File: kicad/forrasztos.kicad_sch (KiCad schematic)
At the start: 58 parts, among them J1 Conn_01x04_Pin, J2 24V+-, J3 Conn_01x06_Pin, J4 Conn_01x20_Pin, Q1 PMOS, Q2 NPN, SW1 RotaryEncoder_Switch, U1 STM32F103C8Tx, U2 24LC00, U3 MCP601R, U4 ATA00A18S-L, U5 AP1117-33, U6 MCP601R, U7 MCP601R, Y1 8 MHz

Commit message: schematic mostly done
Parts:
- removed D3: LED, symbol Device:LED
- removed R14, R15: 10k, symbol Device:R
- removed R16: 470k, symbol Device:R
- removed R17, R19: 1k, symbol Device:R
- removed R18: 4k7, symbol Device:R
- removed R6: 10, symbol Device:R
- removed U3, U6, U7: MCP601R, Package_TO_SOT_SMD:SOT-23-5, symbol Amplifier_Operational:MCP601R
- removed U4: ATA00A18S-L, Converter_DCDC:Converter_DCDC_Artesyn_ATA_SMD, symbol Converter_DCDC:ATA00A18S-L
- removed U5: AP1117-33, Package_TO_SOT_SMD:SOT-223-3_TabPin2, symbol Regulator_Linear:AP1117-33
- removed Y1: 8 MHz, symbol Device:Crystal
- added C15, C16, C21: 100n, Capacitor_SMD:C_0603_1608Metric_Pad1.08x0.95mm_HandSolder, symbol Device:C
- added C17, C22: 22p, Capacitor_SMD:C_0603_1608Metric_Pad1.08x0.95mm_HandSolder, symbol Device:C
- added C18, C19: 1n, Capacitor_SMD:C_0603_1608Metric_Pad1.08x0.95mm_HandSolder, symbol Device:C
- added C6: 22u, Capacitor_SMD:C_0603_1608Metric_Pad1.08x0.95mm_HandSolder, symbol Device:C
- added D4: LED, LED_SMD:LED_1206_3216Metric_Pad1.42x1.75mm_HandSolder, symbol Device:LED
- added L1, L2: 4.7u, Inductor_SMD:L_0603_1608Metric_Pad1.05x0.95mm_HandSolder, symbol Device:L
- added R11, R4: 470k, Resistor_SMD:R_0603_1608Metric_Pad0.98x0.95mm_HandSolder, symbol Device:R
- added R13: 10, Resistor_SMD:R_0603_1608Metric_Pad0.98x0.95mm_HandSolder, symbol Device:R
- added R2, R3: 10k, Resistor_SMD:R_0603_1608Metric_Pad0.98x0.95mm_HandSolder, symbol Device:R
- added RV1: R_Potentiometer, Potentiometer_SMD:Potentiometer_ACP_CA6-VSMD_Vertical, symbol Device:R_Potentiometer
- added U1: AP63205WU, Package_TO_SOT_SMD:TSOT-23-6, symbol Regulator_Switching:AP63200WU
- added U2: AP63203WU, Package_TO_SOT_SMD:TSOT-23-6, symbol Regulator_Switching:AP63203WU
- added U4: MCP602, Package_DIP:DIP-8_W7.62mm_SMDSocket_SmallPads, symbol Amplifier_Operational:MCP602
- added Y1: ABM3B-8.000MHZ-B-2-T, ABM3B8000MHZB2T, symbol ABM3B-8_000MHZ-B-2-T:ABM3B-8.000MHZ-B-2-T
- C1, C4: value 100n -> 10u; footprint (none) -> Capacitor_SMD:C_0603_1608Metric_Pad1.08x0.95mm_HandSolder
- C10, C11, C2, C3, C9: footprint (none) -> Capacitor_SMD:C_0603_1608Metric_Pad1.08x0.95mm_HandSolder
- C12: value 1n -> 10u; footprint (none) -> Capacitor_SMD:C_0603_1608Metric_Pad1.08x0.95mm_HandSolder
- C13, C14: value 1n -> 22u; footprint (none) -> Capacitor_SMD:C_0603_1608Metric_Pad1.08x0.95mm_HandSolder
- C20: renamed from C6; footprint (none) -> Capacitor_SMD:C_0603_1608Metric_Pad1.08x0.95mm_HandSolder
- C5: value 100n -> 22u; footprint (none) -> Capacitor_SMD:C_0603_1608Metric_Pad1.08x0.95mm_HandSolder
- C7: value 22pF -> 10u; footprint (none) -> Capacitor_SMD:C_0603_1608Metric_Pad1.08x0.95mm_HandSolder
- C8: value 22pF -> 100n; footprint (none) -> Capacitor_SMD:C_0603_1608Metric_Pad1.08x0.95mm_HandSolder
- D1: renamed from D4; footprint (none) -> LED_SMD:LED_1206_3216Metric_Pad1.42x1.75mm_HandSolder
- D2: renamed from D1; footprint (none) -> Diode_SMD:D_1206_3216Metric_Pad1.42x1.75mm_HandSolder
- D3: renamed from D2; footprint (none) -> Diode_SMD:D_1206_3216Metric_Pad1.42x1.75mm_HandSolder
- FB1: renamed from FB2; value FerriteBead -> FBMJ4516HS111-T; footprint (none) -> PCM_Ferrite_SMD_Handsoldering_AKL:Ferrite_1806_4516Metric_Pad1.57x1.80mm_BigPads
- FB2: renamed from FB1; value FerriteBead -> FBMJ4516HS111-T; footprint (none) -> PCM_Ferrite_SMD_Handsoldering_AKL:Ferrite_1806_4516Metric_Pad1.57x1.80mm_BigPads
- J1: renamed from J2; footprint (none) -> Connector_PinHeader_2.54mm:PinHeader_1x02_P2.54mm_Vertical
- J2: renamed from J4; footprint (none) -> Connector_PinHeader_2.54mm:PinHeader_1x20_P2.54mm_Vertical
- J3: footprint (none) -> Connector_PinHeader_2.54mm:PinHeader_1x06_P2.54mm_Vertical
- J4: renamed from J1; footprint (none) -> Connector_PinHeader_2.54mm:PinHeader_1x04_P2.54mm_Vertical
- Q1: value PMOS -> AOD409; footprint (none) -> Library:TO-252-2-custom
- Q2: value NPN -> MMST2222A; footprint (none) -> Package_TO_SOT_SMD:SOT-323_SC-70_Handsoldering
- R1: renamed from R13; footprint (none) -> Resistor_SMD:R_0603_1608Metric_Pad0.98x0.95mm_HandSolder
- R10: value 470k -> 1M; footprint (none) -> Resistor_SMD:R_0603_1608Metric_Pad0.98x0.95mm_HandSolder
- R12: renamed from R21; footprint (none) -> Resistor_SMD:R_0603_1608Metric_Pad0.98x0.95mm_HandSolder
- R14: renamed from R2; value 2k -> 390; footprint (none) -> Resistor_SMD:R_1206_3216Metric_Pad1.30x1.75mm_HandSolder
- R15: renamed from R22; footprint (none) -> Resistor_SMD:R_0603_1608Metric_Pad0.98x0.95mm_HandSolder
- R16: renamed from R23; footprint (none) -> Resistor_SMD:R_0603_1608Metric_Pad0.98x0.95mm_HandSolder
- R17: renamed from R20; footprint (none) -> Resistor_SMD:R_1206_3216Metric_Pad1.30x1.75mm_HandSolder
- R18: renamed from R3; value 1k -> 390; footprint (none) -> Resistor_SMD:R_1206_3216Metric_Pad1.30x1.75mm_HandSolder
- R19: renamed from R12; footprint (none) -> Resistor_SMD:R_0603_1608Metric_Pad0.98x0.95mm_HandSolder
- R20: renamed from R11; footprint (none) -> Resistor_SMD:R_0603_1608Metric_Pad0.98x0.95mm_HandSolder
- R21: renamed from R4; footprint (none) -> Resistor_SMD:R_1206_3216Metric_Pad1.30x1.75mm_HandSolder
- R5: value 30k -> 1M; footprint (none) -> Resistor_SMD:R_0603_1608Metric_Pad0.98x0.95mm_HandSolder
- R6: renamed from R9; value 10k -> 5k; footprint (none) -> Resistor_SMD:R_1206_3216Metric_Pad1.30x1.75mm_HandSolder
- R7: footprint (none) -> Resistor_SMD:R_0603_1608Metric_Pad0.98x0.95mm_HandSolder
- R8: value 10k -> 5k; footprint (none) -> Resistor_SMD:R_1206_3216Metric_Pad1.30x1.75mm_HandSolder
- R9: renamed from R1; footprint (none) -> Resistor_SMD:R_0603_1608Metric_Pad0.98x0.95mm_HandSolder
- SW1: footprint (none) -> Rotary_Encoder:RotaryEncoder_Alps_EC12E_Vertical_H20mm
- U3: renamed from U2; footprint (none) -> Package_DIP:DIP-8_W7.62mm
- renumbered U1 to U5
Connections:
- net +24V: now also C4.1, Q1.1 (D), U1.2 (EN), U1.3 (IN); no longer Q1.3 (S)
- net +3.3V: now also C10.1, C11.1, C13.1, C14.1, C8.1, C9.1, C15.1, L2.2, R2.1, R3.1, U2.1 (FB); no longer C1.1, C2.1, C3.1, C4.1, C5.1, J2.2 (Pin_2)
- net +3.3VA: now also C16.1; no longer C9.1
- net +5V: now also C12.1, C2.1, C5.1, J2.19 (Pin_19), J2.2 (Pin_2), C21.1, C6.1, L1.2, RV1.1, U1.1 (FB), U2.2 (EN), U2.3 (IN); no longer C10.1
- net +5VA: now also C3.1, U4.8 (V+); no longer C11.1
- net CURR: now also D4.2 (A), U4.7
- net DIFFAMP_P: now also Q1.3 (S); no longer D2.2 (A), Q1.1 (D)
- net ENC_A: now also C19.1, R3.2; no longer C12.1
- net ENC_B: now also C18.1, R2.2; no longer C13.1
- net GND: now also C8.2, J2.20 (Pin_20), SW1.S1, C15.2, C16.2, C17.1, C18.2, C19.2, C22.1, C6.2, D4.1 (K), R4.2, U1.4 (GND), U2.4 (GND), U4.4 (V-), Y1.2 (GND_1), Y1.4 (GND_2); no longer C1.2, C7.1, C8.1, D2.1 (K), D3.2 (A), R5.2, R8.2
- net LCD_CS1: now also J2.15 (Pin_15), U5.20 (PB2); no longer U5.19 (PB1)
- net LCD_CS2: now also J2.16 (Pin_16), U5.19 (PB1); no longer U5.20 (PB2)
- net LCD_D0: now also U5.30 (PA9); no longer U5.29 (PA8)
- net LCD_D1: now also U5.29 (PA8); no longer U5.30 (PA9)
- net LCD_D2: now also U5.28 (PB15); no longer U5.21 (PB10)
- net LCD_D3: now also U5.27 (PB14); no longer U5.22 (PB11)
- net LCD_D4: now also U5.26 (PB13); no longer U5.25 (PB12)
- net LCD_D5: now also U5.25 (PB12); no longer U5.26 (PB13)
- net LCD_D6: now also U5.22 (PB11); no longer U5.27 (PB14)
- net LCD_D7: now also U5.21 (PB10); no longer U5.28 (PB15)
- net LCD_E: now also U5.31 (PA10); no longer U5.15 (PA5)
- net LCD_RW: now also U5.32 (PA11); no longer U5.16 (PA6)
- net TEMP: now also D1.2 (A), R10.2, U4.1
- net at R6.1: now also D2.2 (A), R5.2, U4.3 (+)
- net at R10.1: now also R11.1; no longer R8.1
- net at R12.1: now also U4.5 (+)
- net LCD_VOUT: now reaches J2.18 (Pin_18)
- net LCD_VOUT: now also RV1.3
- net LCD_V0: now reaches J2.3 (Pin_3)
- net LCD_V0: now also C21.2, RV1.2
- net at R15.1, R16.1: now also U4.6 (-)
- net LCD_DI: now reaches U5.33 (PA12)
- net LCD_DI: now also J2.4 (Pin_4)
- net at C7.2: now also L2.1, U2.5 (SW); no longer U5.5 (PD0)
- net CRYSTAL_2: now reaches U5.6 (PD1)
- net CRYSTAL_2: now also R13.2
- net at Q2.2 (B), R21.1: no longer R5.1
- net CURRAMP renamed DIFFAMP_N
- net DIFFAMP_N: now also R8.2
- net LCD_RS: no longer names the net of U5.17 (PA7)
- net LCD_RS: no longer J2.4 (Pin_4)
- net sensor renamed TILT
- new net: D2.1 (K), D3.2 (A), R11.2, R8.1, U4.2 (-)
- new net: C7.1, U2.6 (BST)
- new net: C1.2, L1.1, U1.5 (SW)
- new net: C1.1, U1.6 (BST)
- new net: R4.1, R5.1
- new net: C22.2, R13.1, Y1.3 (CRYSTAL_2)
- new net CRYSTAL_1: C17.2, U5.5 (PD0), Y1.1 (CRYSTAL_1)
- no-connect marks 0 -> 9
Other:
- moved on the sheet: C20, D1, D2, D3, FB1, FB2, J1, J2, J3, J4, Q2, R10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

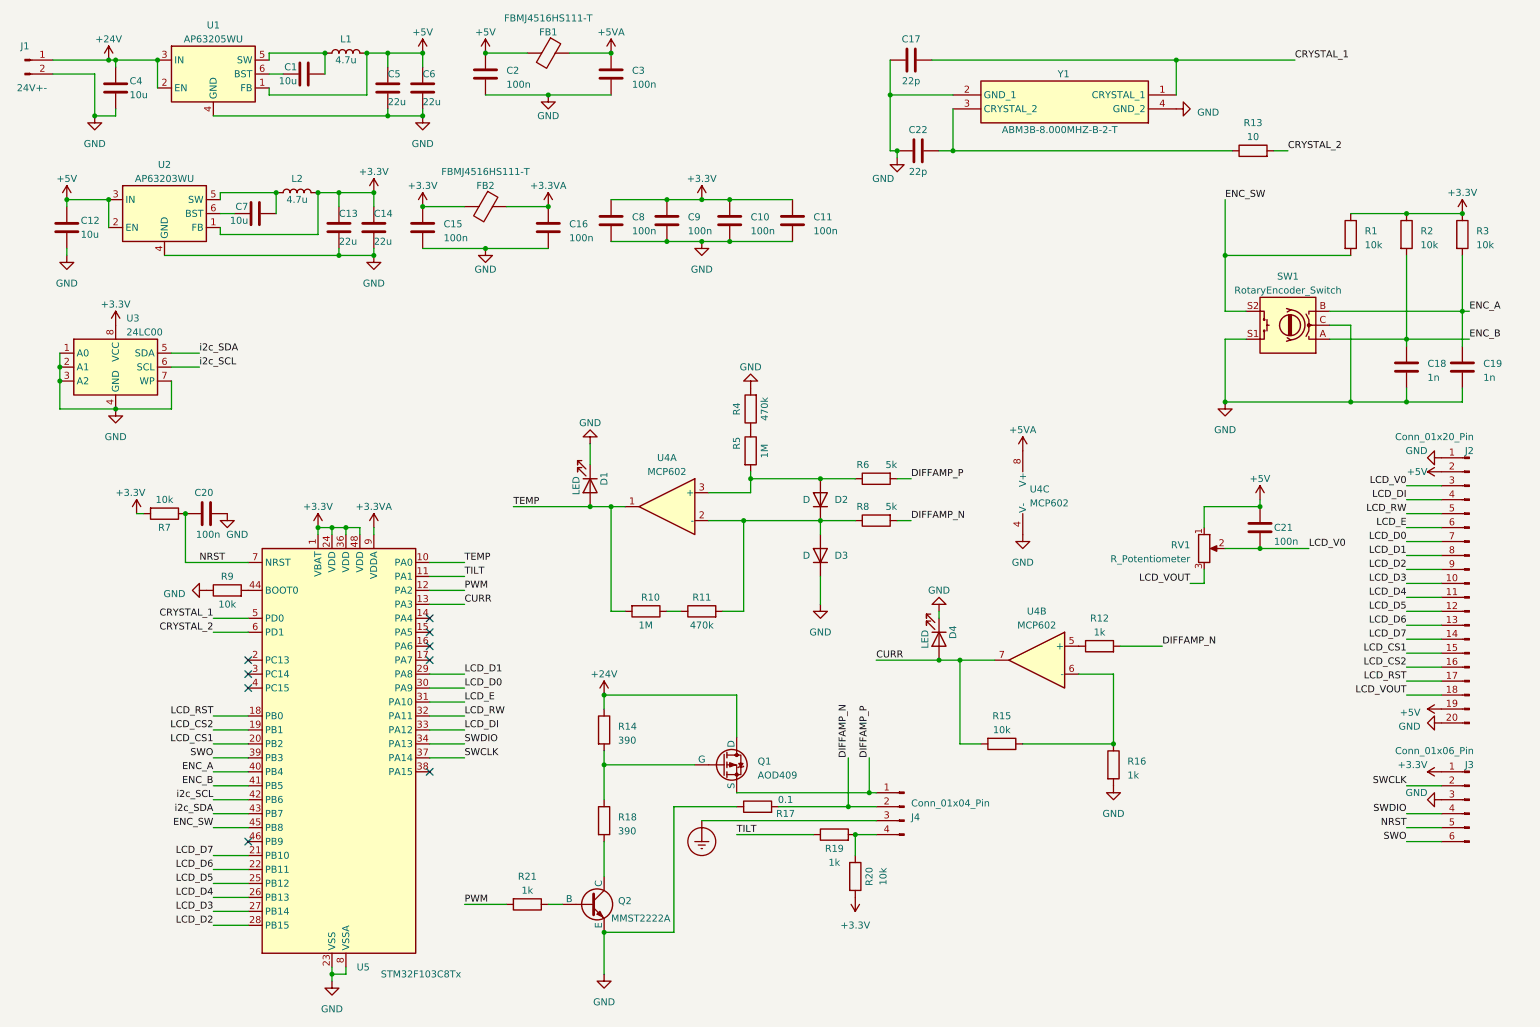
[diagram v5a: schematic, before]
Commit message: added 2nd channel
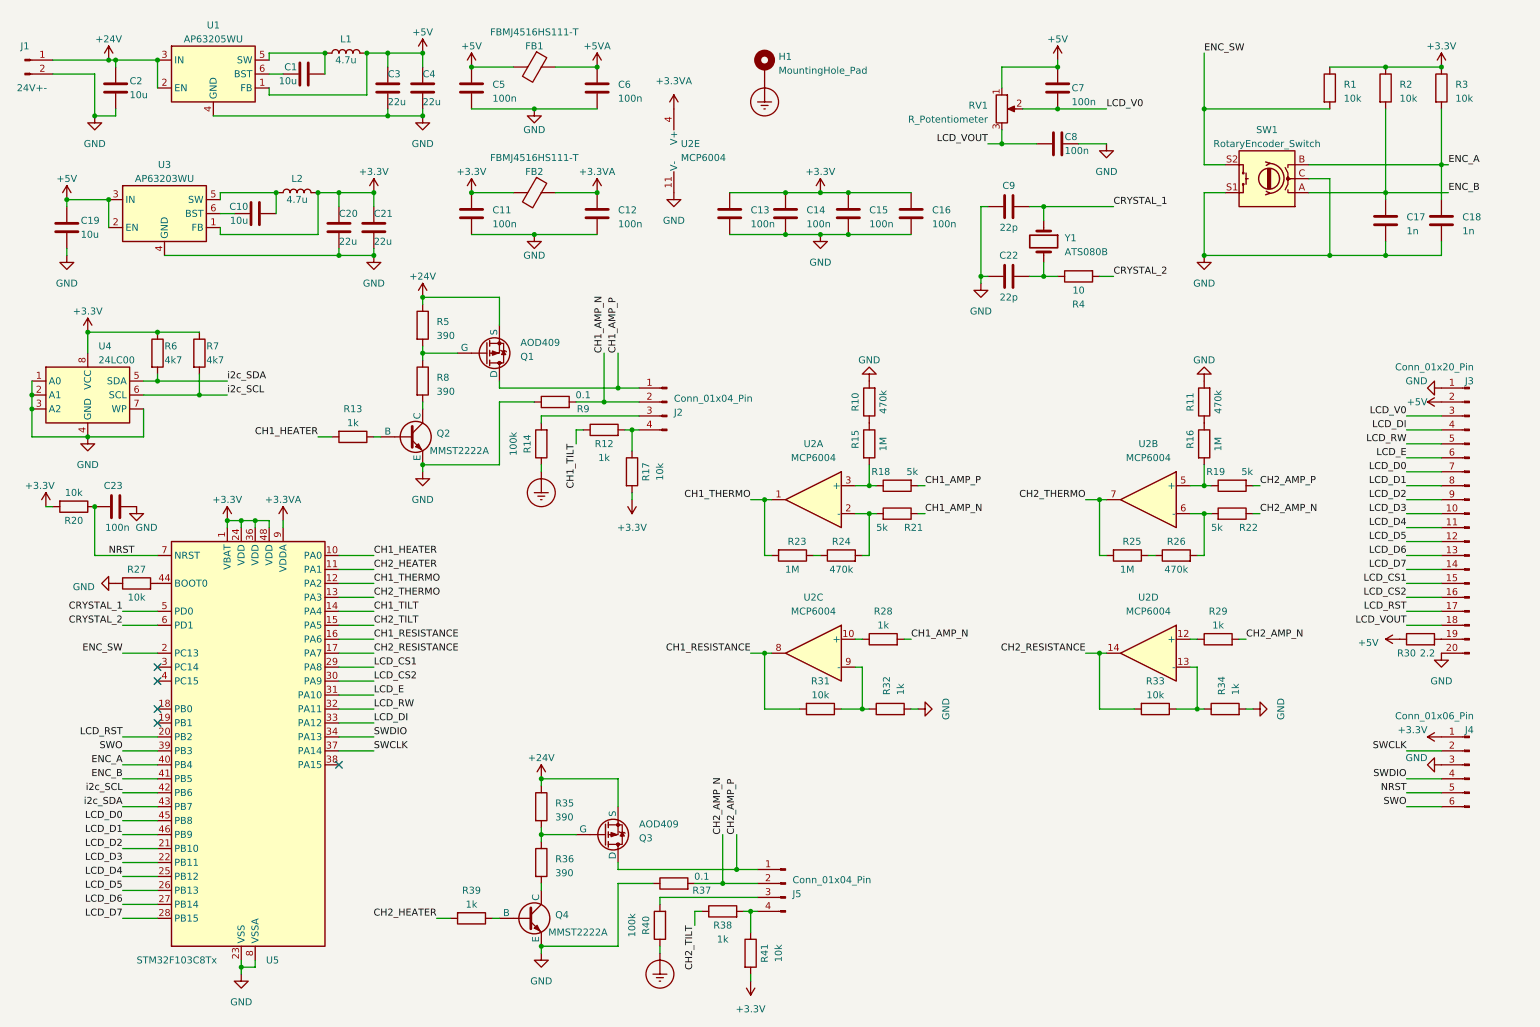
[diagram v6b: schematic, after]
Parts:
- removed C17: 22p, Capacitor_SMD:C_0603_1608Metric_Pad1.08x0.95mm_HandSolder, symbol Device:C
- removed D1, D4: LED, LED_SMD:LED_1206_3216Metric_Pad1.42x1.75mm_HandSolder, symbol Device:LED
- removed D2, D3: D, Diode_SMD:D_1206_3216Metric_Pad1.42x1.75mm_HandSolder, symbol Device:D
- removed U4: MCP602, Package_DIP:DIP-8_W7.62mm_SMDSocket_SmallPads, symbol Amplifier_Operational:MCP602
- removed Y1: ABM3B-8.000MHZ-B-2-T, ABM3B8000MHZB2T, symbol ABM3B-8_000MHZ-B-2-T:ABM3B-8.000MHZ-B-2-T
- added C8: 100n, Capacitor_SMD:C_0805_2012Metric_Pad1.18x1.45mm_HandSolder, symbol Device:C
- added C9: 22p, Capacitor_SMD:C_0805_2012Metric_Pad1.18x1.45mm_HandSolder, symbol Device:C
- added H1: MountingHole_Pad, symbol Mechanical:MountingHole_Pad
- added J2: Conn_01x04_Pin, Connector_PinHeader_2.54mm:PinHeader_1x04_P2.54mm_Vertical, symbol Connector:Conn_01x04_Pin
- added Q2: MMST2222A, Package_TO_SOT_SMD:SOT-323_SC-70_Handsoldering, symbol Simulation_SPICE:NPN
- added Q3: AOD409, Library:TO-252-2-custom, symbol Simulation_SPICE:PMOS
- added R11, R26: 470k, Resistor_SMD:R_0805_2012Metric_Pad1.20x1.40mm_HandSolder, symbol Device:R
- added R12, R29, R34: 1k, Resistor_SMD:R_0805_2012Metric_Pad1.20x1.40mm_HandSolder, symbol Device:R
- added R14, R40: 100k, Resistor_THT:R_Axial_DIN0207_L6.3mm_D2.5mm_P10.16mm_Horizontal, symbol Device:R
- added R16, R25: 1M, Resistor_SMD:R_0805_2012Metric_Pad1.20x1.40mm_HandSolder, symbol Device:R
- added R17, R33: 10k, Resistor_SMD:R_0805_2012Metric_Pad1.20x1.40mm_HandSolder, symbol Device:R
- added R19, R22: 5k, Resistor_SMD:R_0805_2012Metric_Pad1.20x1.40mm_HandSolder, symbol Device:R
- added R30: 2.2, Resistor_THT:R_Axial_DIN0207_L6.3mm_D2.5mm_P10.16mm_Horizontal, symbol Device:R
- added R4: 10, Resistor_SMD:R_0805_2012Metric_Pad1.20x1.40mm_HandSolder, symbol Device:R
- added R5, R8: 390, Resistor_SMD:R_0805_2012Metric_Pad1.20x1.40mm_HandSolder, symbol Device:R
- added R6, R7: 4k7, Resistor_SMD:R_0805_2012Metric_Pad1.20x1.40mm_HandSolder, symbol Device:R
- added R9: 0.1, Resistor_SMD:R_0805_2012Metric_Pad1.20x1.40mm_HandSolder, symbol Device:R
- added U2: MCP6004, Package_SO:SOIC-14_3.9x8.7mm_P1.27mm, symbol Amplifier_Operational:MCP6004
- added Y1: ATS080B, Crystal:Crystal_HC49-U_Vertical, symbol Device:Crystal
- C1: footprint Capacitor_SMD:C_0603_1608Metric_Pad1.08x0.95mm_HandSolder -> Capacitor_SMD:C_1206_3216Metric_Pad1.33x1.80mm_HandSolder
- C10: renamed from C7; footprint Capacitor_SMD:C_0603_1608Metric_Pad1.08x0.95mm_HandSolder -> Capacitor_SMD:C_1206_3216Metric_Pad1.33x1.80mm_HandSolder
- C11: renamed from C15; footprint Capacitor_SMD:C_0603_1608Metric_Pad1.08x0.95mm_HandSolder -> Capacitor_SMD:C_0805_2012Metric_Pad1.18x1.45mm_HandSolder
- C12: renamed from C16; footprint Capacitor_SMD:C_0603_1608Metric_Pad1.08x0.95mm_HandSolder -> Capacitor_SMD:C_0805_2012Metric_Pad1.18x1.45mm_HandSolder
- C13: renamed from C8; footprint Capacitor_SMD:C_0603_1608Metric_Pad1.08x0.95mm_HandSolder -> Capacitor_SMD:C_0805_2012Metric_Pad1.18x1.45mm_HandSolder
- C14: renamed from C9; footprint Capacitor_SMD:C_0603_1608Metric_Pad1.08x0.95mm_HandSolder -> Capacitor_SMD:C_0805_2012Metric_Pad1.18x1.45mm_HandSolder
- C15: renamed from C10; footprint Capacitor_SMD:C_0603_1608Metric_Pad1.08x0.95mm_HandSolder -> Capacitor_SMD:C_0805_2012Metric_Pad1.18x1.45mm_HandSolder
- C16: renamed from C11; footprint Capacitor_SMD:C_0603_1608Metric_Pad1.08x0.95mm_HandSolder -> Capacitor_SMD:C_0805_2012Metric_Pad1.18x1.45mm_HandSolder
- C17: renamed from C18; footprint Capacitor_SMD:C_0603_1608Metric_Pad1.08x0.95mm_HandSolder -> Capacitor_SMD:C_0805_2012Metric_Pad1.18x1.45mm_HandSolder
- C18: renamed from C19; footprint Capacitor_SMD:C_0603_1608Metric_Pad1.08x0.95mm_HandSolder -> Capacitor_SMD:C_0805_2012Metric_Pad1.18x1.45mm_HandSolder
- C19: renamed from C12; footprint Capacitor_SMD:C_0603_1608Metric_Pad1.08x0.95mm_HandSolder -> Capacitor_SMD:C_1206_3216Metric_Pad1.33x1.80mm_HandSolder
- C2: renamed from C4; footprint Capacitor_SMD:C_0603_1608Metric_Pad1.08x0.95mm_HandSolder -> Capacitor_SMD:C_1206_3216Metric_Pad1.33x1.80mm_HandSolder
- C20: renamed from C13; footprint Capacitor_SMD:C_0603_1608Metric_Pad1.08x0.95mm_HandSolder -> Capacitor_SMD:C_1206_3216Metric_Pad1.33x1.80mm_HandSolder
- C21: renamed from C14; footprint Capacitor_SMD:C_0603_1608Metric_Pad1.08x0.95mm_HandSolder -> Capacitor_SMD:C_1206_3216Metric_Pad1.33x1.80mm_HandSolder
- C22: footprint Capacitor_SMD:C_0603_1608Metric_Pad1.08x0.95mm_HandSolder -> Capacitor_SMD:C_0805_2012Metric_Pad1.18x1.45mm_HandSolder
- C23: renamed from C20; footprint Capacitor_SMD:C_0603_1608Metric_Pad1.08x0.95mm_HandSolder -> Capacitor_SMD:C_0805_2012Metric_Pad1.18x1.45mm_HandSolder
- C3: renamed from C5; footprint Capacitor_SMD:C_0603_1608Metric_Pad1.08x0.95mm_HandSolder -> Capacitor_SMD:C_1206_3216Metric_Pad1.33x1.80mm_HandSolder
- C4: renamed from C6; footprint Capacitor_SMD:C_0603_1608Metric_Pad1.08x0.95mm_HandSolder -> Capacitor_SMD:C_1206_3216Metric_Pad1.33x1.80mm_HandSolder
- C5: renamed from C2; footprint Capacitor_SMD:C_0603_1608Metric_Pad1.08x0.95mm_HandSolder -> Capacitor_SMD:C_0805_2012Metric_Pad1.18x1.45mm_HandSolder
- C6: renamed from C3; footprint Capacitor_SMD:C_0603_1608Metric_Pad1.08x0.95mm_HandSolder -> Capacitor_SMD:C_0805_2012Metric_Pad1.18x1.45mm_HandSolder
- C7: renamed from C21; footprint Capacitor_SMD:C_0603_1608Metric_Pad1.08x0.95mm_HandSolder -> Capacitor_SMD:C_0805_2012Metric_Pad1.18x1.45mm_HandSolder
- R1, R2, R3: footprint Resistor_SMD:R_0603_1608Metric_Pad0.98x0.95mm_HandSolder -> Resistor_SMD:R_0805_2012Metric_Pad1.20x1.40mm_HandSolder
- R10: renamed from R4; footprint Resistor_SMD:R_0603_1608Metric_Pad0.98x0.95mm_HandSolder -> Resistor_SMD:R_0805_2012Metric_Pad1.20x1.40mm_HandSolder
- R13: value 10 -> 1k; footprint Resistor_SMD:R_0603_1608Metric_Pad0.98x0.95mm_HandSolder -> Resistor_SMD:R_0805_2012Metric_Pad1.20x1.40mm_HandSolder
- R15: renamed from R5; footprint Resistor_SMD:R_0603_1608Metric_Pad0.98x0.95mm_HandSolder -> Resistor_SMD:R_0805_2012Metric_Pad1.20x1.40mm_HandSolder
- R18: renamed from R6; footprint Resistor_SMD:R_1206_3216Metric_Pad1.30x1.75mm_HandSolder -> Resistor_SMD:R_0805_2012Metric_Pad1.20x1.40mm_HandSolder
- R20: renamed from R7; footprint Resistor_SMD:R_0603_1608Metric_Pad0.98x0.95mm_HandSolder -> Resistor_SMD:R_0805_2012Metric_Pad1.20x1.40mm_HandSolder
- R21: renamed from R8; footprint Resistor_SMD:R_1206_3216Metric_Pad1.30x1.75mm_HandSolder -> Resistor_SMD:R_0805_2012Metric_Pad1.20x1.40mm_HandSolder
- R23: renamed from R10; footprint Resistor_SMD:R_0603_1608Metric_Pad0.98x0.95mm_HandSolder -> Resistor_SMD:R_0805_2012Metric_Pad1.20x1.40mm_HandSolder
- R24: renamed from R11; footprint Resistor_SMD:R_0603_1608Metric_Pad0.98x0.95mm_HandSolder -> Resistor_SMD:R_0805_2012Metric_Pad1.20x1.40mm_HandSolder
- R27: renamed from R9; footprint Resistor_SMD:R_0603_1608Metric_Pad0.98x0.95mm_HandSolder -> Resistor_SMD:R_0805_2012Metric_Pad1.20x1.40mm_HandSolder
- R28: renamed from R12; footprint Resistor_SMD:R_0603_1608Metric_Pad0.98x0.95mm_HandSolder -> Resistor_SMD:R_0805_2012Metric_Pad1.20x1.40mm_HandSolder
- R31: renamed from R15; footprint Resistor_SMD:R_0603_1608Metric_Pad0.98x0.95mm_HandSolder -> Resistor_SMD:R_0805_2012Metric_Pad1.20x1.40mm_HandSolder
- R32: renamed from R16; footprint Resistor_SMD:R_0603_1608Metric_Pad0.98x0.95mm_HandSolder -> Resistor_SMD:R_0805_2012Metric_Pad1.20x1.40mm_HandSolder
- R35: renamed from R14; footprint Resistor_SMD:R_1206_3216Metric_Pad1.30x1.75mm_HandSolder -> Resistor_SMD:R_0805_2012Metric_Pad1.20x1.40mm_HandSolder
- R36: renamed from R18; footprint Resistor_SMD:R_1206_3216Metric_Pad1.30x1.75mm_HandSolder -> Resistor_SMD:R_0805_2012Metric_Pad1.20x1.40mm_HandSolder
- R37: renamed from R17; footprint Resistor_SMD:R_1206_3216Metric_Pad1.30x1.75mm_HandSolder -> Resistor_SMD:R_0805_2012Metric_Pad1.20x1.40mm_HandSolder
- R38: renamed from R19; footprint Resistor_SMD:R_0603_1608Metric_Pad0.98x0.95mm_HandSolder -> Resistor_SMD:R_0805_2012Metric_Pad1.20x1.40mm_HandSolder
- R39: renamed from R21; footprint Resistor_SMD:R_1206_3216Metric_Pad1.30x1.75mm_HandSolder -> Resistor_SMD:R_0805_2012Metric_Pad1.20x1.40mm_HandSolder
- R41: renamed from R20; footprint Resistor_SMD:R_0603_1608Metric_Pad0.98x0.95mm_HandSolder -> Resistor_SMD:R_0805_2012Metric_Pad1.20x1.40mm_HandSolder
- renumbered J2 to J3, J3 to J4, J4 to J5, Q2 to Q4, U2 to U3, U3 to U4
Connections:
- net +24V: now also Q1.3 (S), Q3.3 (S), R5.1; no longer Q1.1 (D)
- net +3.3V: now also R17.2, R6.1, R7.1
- net +3.3VA: now also U2.4 (V+)
- net +5V: now also R30.1; no longer J3.19 (Pin_19)
- net CRYSTAL_1: now also C9.2, Y1.1
- net CRYSTAL_2: now also R4.2; no longer R13.2
- net ENC_SW: now also U5.2 (PC13); no longer U5.45 (PB8)
- net Earth_Protective: now also H1.1, R14.1, R40.1; no longer J5.3 (Pin_3)
- net GND: now also C8.1, C9.1, Q2.3 (E), R11.2, R34.2, R9.1, U2.11 (V-)
- net LCD_CS1: now also U5.29 (PA8); no longer U5.20 (PB2)
- net LCD_CS2: now also U5.30 (PA9); no longer U5.19 (PB1)
- net LCD_D0: now also U5.45 (PB8); no longer U5.30 (PA9)
- net LCD_D1: now also U5.46 (PB9); no longer U5.29 (PA8)
- net LCD_D2: now also U5.21 (PB10); no longer U5.28 (PB15)
- net LCD_D3: now also U5.22 (PB11); no longer U5.27 (PB14)
- net LCD_D4: now also U5.25 (PB12); no longer U5.26 (PB13)
- net LCD_D5: now also U5.26 (PB13); no longer U5.25 (PB12)
- net LCD_D6: now also U5.27 (PB14); no longer U5.22 (PB11)
- net LCD_D7: now also U5.28 (PB15); no longer U5.21 (PB10)
- net LCD_RST: now also U5.20 (PB2); no longer U5.18 (PB0)
- net LCD_VOUT: now also C8.2
- net i2c_SCL: now also R7.2
- net i2c_SDA: now also R6.2
- net at R24.2: now also R21.2, U2.2 (-); no longer R21.1
- net at R28.1: now also U2.10 (+)
- net CH1_TILT: now reaches U5.14 (PA4)
- net CH1_TILT: now also R12.1
- net CH2_TILT: now reaches U5.15 (PA5)
- net CH2_TILT: now also R38.1
- net CH1_RESISTANCE: now reaches U5.16 (PA6)
- net CH1_RESISTANCE: now also R31.2, U2.8
- net CH2_RESISTANCE: now reaches U5.17 (PA7)
- net CH2_RESISTANCE: now also R33.2, U2.14
- net at R35.2, R36.1: now also Q3.2 (G); no longer Q1.2 (G)
- net at R15.2, R18.1: now also U2.3 (+)
- net at R31.1, R32.1: now also U2.9 (-)
- net at R13.1: now also Q2.2 (B); no longer C22.2
- net CURR renamed CH2_THERMO
- net CH2_THERMO: now also R25.2, U2.7; no longer R31.2
- net DIFFAMP_N renamed CH2_AMP_N
- net CH2_AMP_N: now also R22.1, R29.2; no longer R21.2, R28.2
- removed net DIFFAMP_P: J5.1 (Pin_1), Q1.3 (S), R18.2
- net PWM renamed CH1_THERMO
- net CH1_THERMO: now also R23.2, U2.1; no longer R39.2
- net TEMP renamed CH1_HEATER
- net CH1_HEATER: now also R13.2; no longer R23.2
- net TILT renamed CH2_HEATER
- net CH2_HEATER: now also R39.2; no longer R38.1
- new net: J2.3 (Pin_3), R14.2
- new net: R16.2, R19.1, U2.5 (+)
- new net: R29.1, U2.12 (+)
- new net: J3.19 (Pin_19), R30.2
- new net: R33.1, R34.1, U2.13 (-)
- new net: R22.2, R26.2, U2.6 (-)
- new net: J5.3 (Pin_3), R40.2
- new net: R25.1, R26.1
- new net: Q1.2 (G), R5.2, R8.1
- new net: Q2.1 (C), R8.2
- new net: R11.1, R16.1
- new net: C22.2, R4.1, Y1.2
- new net: J2.4 (Pin_4), R12.2, R17.1
- new net CH1_AMP_N: J2.2 (Pin_2), R21.1, R28.2, R9.2
- new net CH1_AMP_P: J2.1 (Pin_1), Q1.1 (D), R18.2
- new net CH2_AMP_P: J5.1 (Pin_1), Q3.1 (D), R19.2
- no-connect marks 9 -> 5
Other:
- moved on the sheet: C11, C12, C13, C14, C15, C16, C17, C18, C23, C5, C6, C7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
